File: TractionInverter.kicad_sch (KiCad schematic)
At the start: 13 parts, among them J1 HV+, J2 HVGND, J3 A_Out, J4 B_Out, J5 C_Out

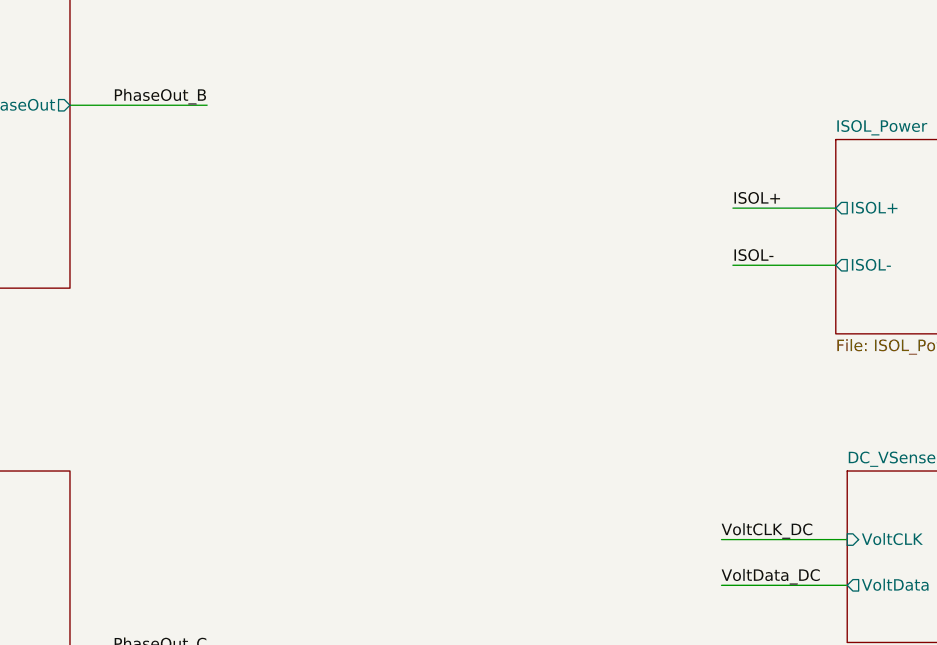
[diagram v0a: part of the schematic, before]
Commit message: new bulk caps, new HV+,- connector placement
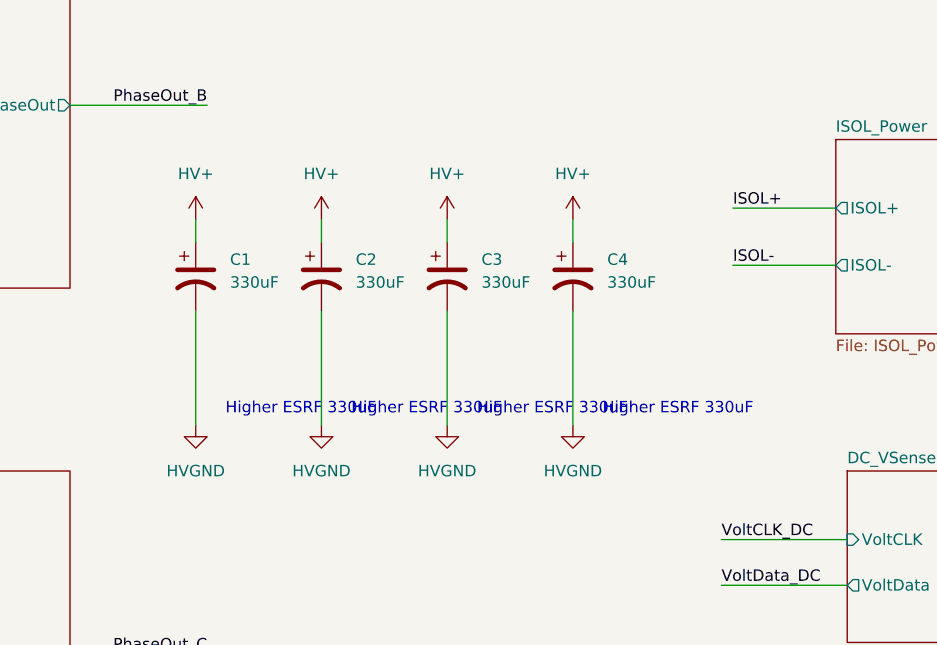
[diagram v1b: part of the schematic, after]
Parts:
- added C1, C2, C3, C4: 330uF, TractionInverter:CAP_UPZ_12P5X50_NCH, symbol Device:C_Polarized_US
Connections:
- net HV+: now also C1.1, C2.1, C3.1, C4.1
- net HVGND: now also C1.2, C2.2, C3.2, C4.2
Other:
- note added: "Higher ESRF 330uF"

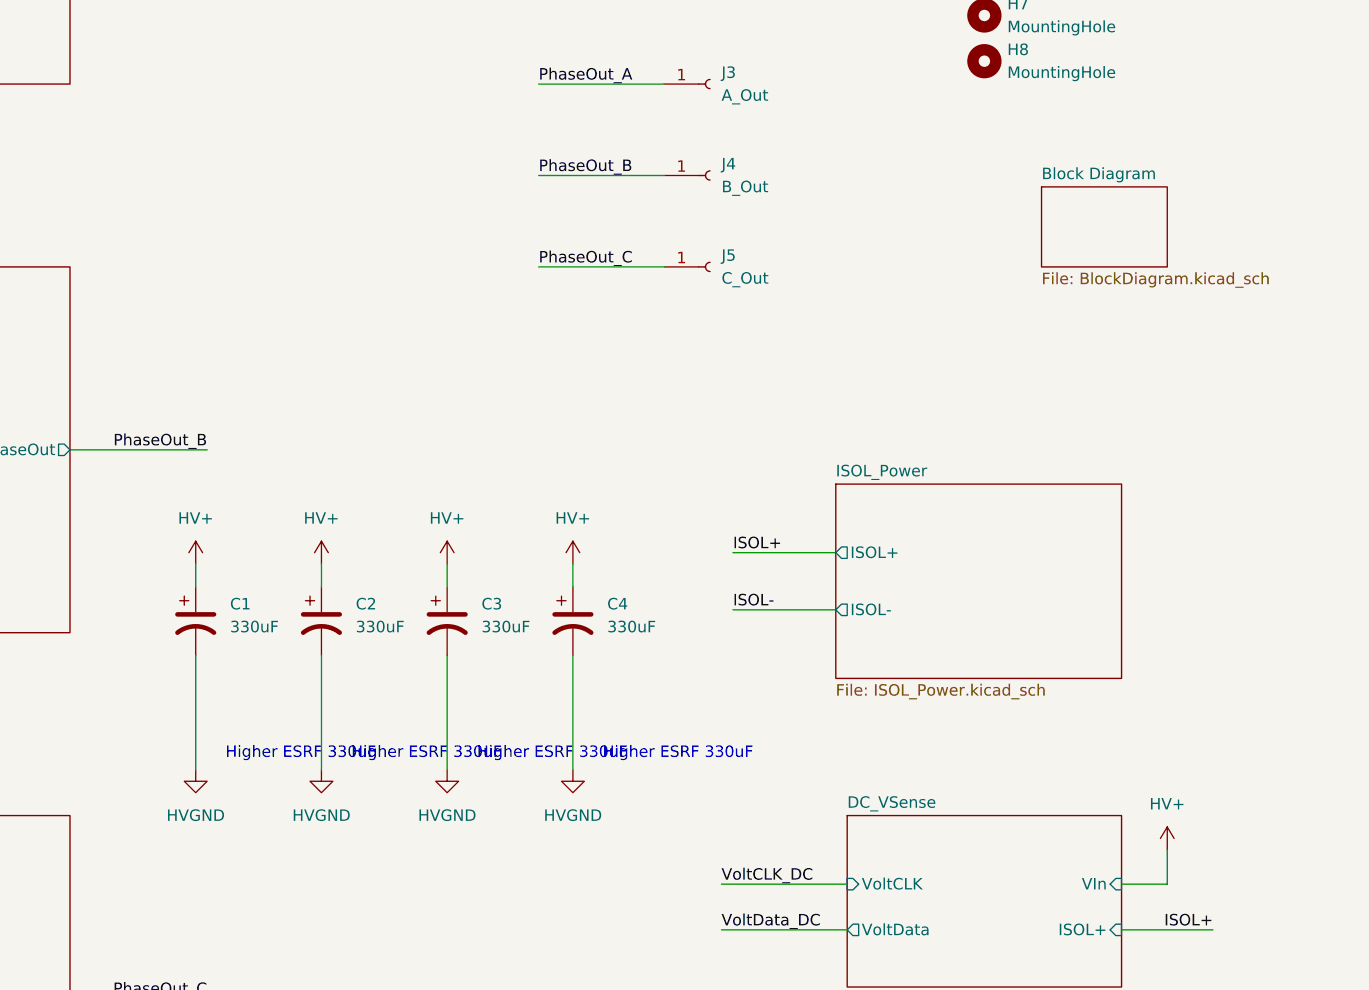
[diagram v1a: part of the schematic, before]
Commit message: bulk caps sheet + adc data clk trace crosstalk
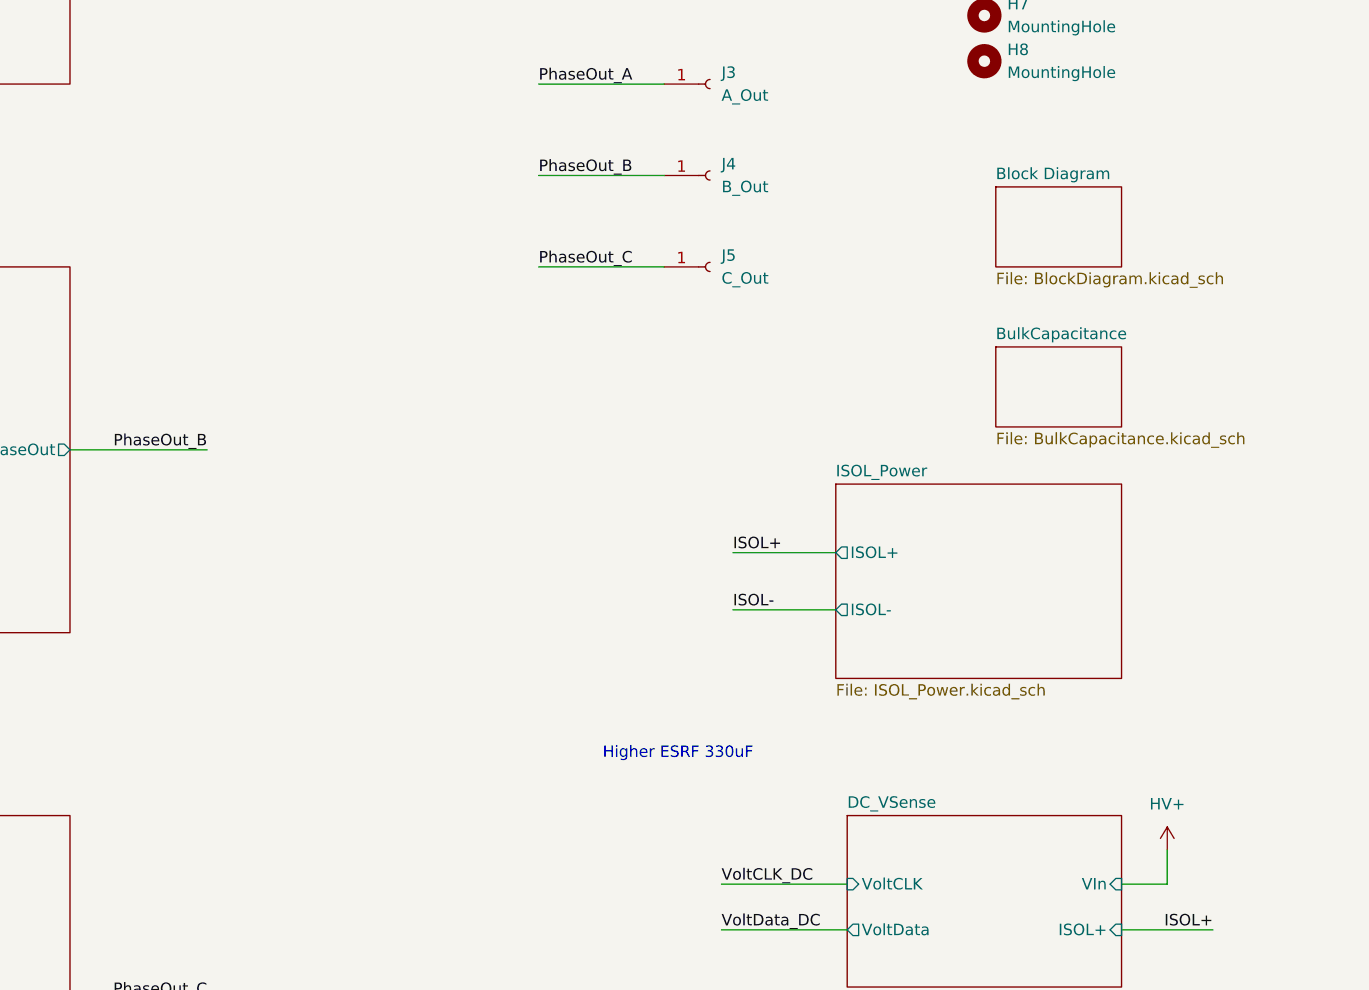
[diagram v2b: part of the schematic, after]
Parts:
- removed C1, C2, C3, C4: 330uF, TractionInverter:CAP_UPZ_12P5X50_NCH, symbol Device:C_Polarized_US
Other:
- added sheet BulkCapacitance (BulkCapacitance.kicad_sch)

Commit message: gate driver connector 1 layout and isodcdc L
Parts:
- renumbered J3 to J1, J1 to J2, J4 to J3, J2 to J4
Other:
- removed sheet LV_Connector_A
- removed sheet LV_Connectors_B
- removed sheet LV_Connectors_C
- added sheet GateDriverConnectors (GateDriverConnectors.kicad_sch)
- note removed: "Higher ESRF 330uF"
- moved on the sheet: H1, H2, H3, H4, H5, H6, H7, H8, J1, J2, J3, J4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

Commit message: need to pass drc
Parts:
- added H10, H9: MountingHole, MountingHole:MountingHole_3mm, symbol Mechanical:MountingHole
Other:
- moved on the sheet: H1, H2, H3, H4, H5, H6, H7, H8
